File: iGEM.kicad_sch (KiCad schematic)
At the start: 57 parts, among them IC1 TMCS1107A1BQDRQ1, IC2 MCP4642-502E_UN, IC3 SN74LVC2G08IDCTRQ1, J1 COIL, J2 Conn_01x03, J3 Conn_01x02, J4 Conn_01x03, J5 Conn_01x03, J6 Conn_02x03_Odd_Even, M1 Fan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

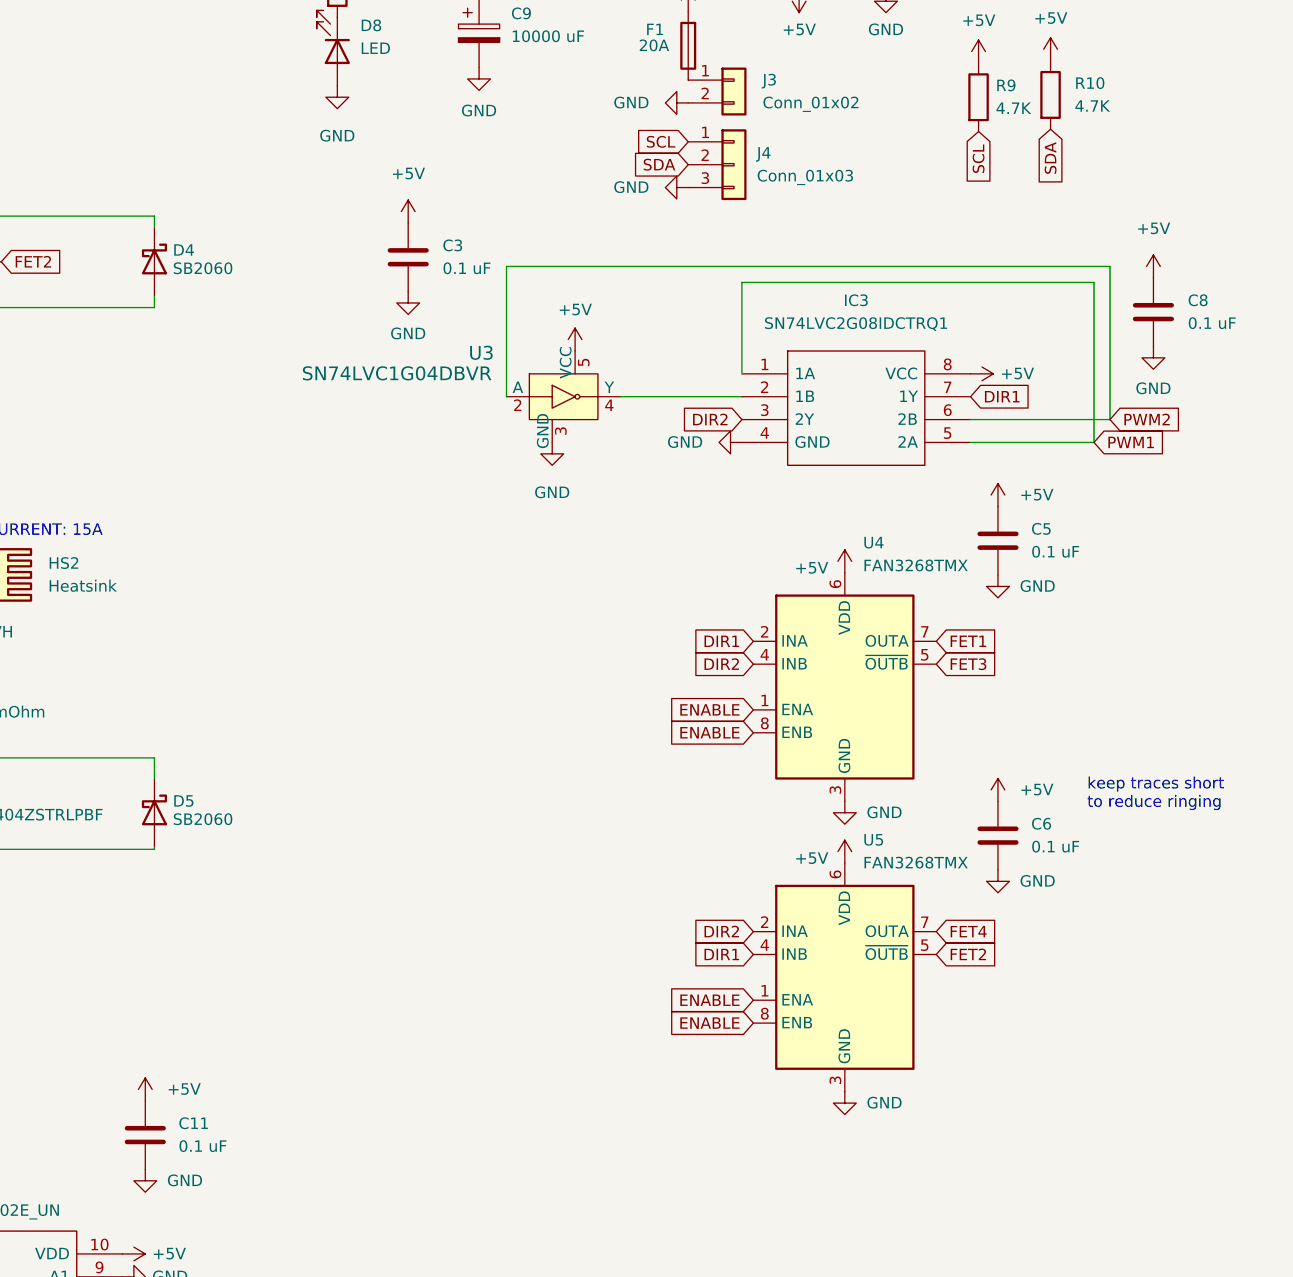
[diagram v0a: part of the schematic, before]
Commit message: MAJOR LOGIC BUG FIX. Layout also altered
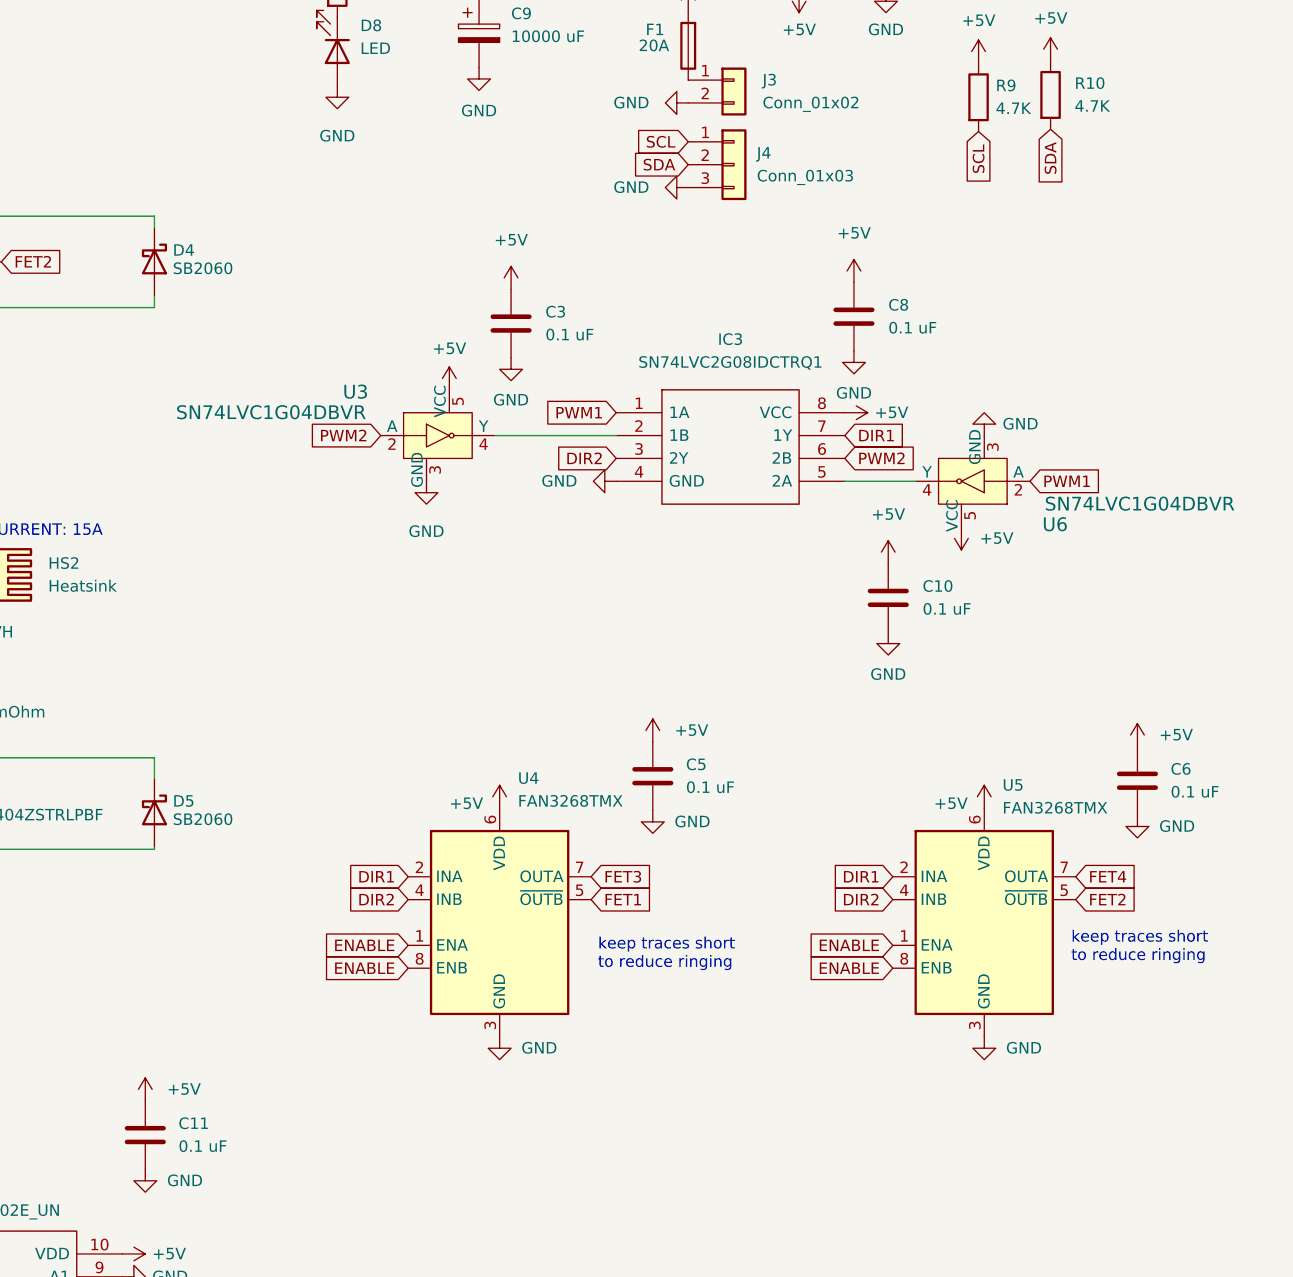
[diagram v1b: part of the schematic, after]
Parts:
- added C10: 0.1 uF, Capacitor_SMD:C_0805_2012Metric_Pad1.18x1.45mm_HandSolder, symbol Device:C
- added U6: SN74LVC1G04DBVR, digikey-footprints:SOT-753, symbol dk_Logic-Gates-and-Inverters:SN74LVC1G04DBVR
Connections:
- net +5V: now also C10.1, U6.5 (VCC)
- net DIR1: now also U5.2 (INA); no longer U5.4 (INB)
- net DIR2: now also U5.4 (INB); no longer U5.2 (INA)
- net FET1: now also U4.5 (~{OUTB}); no longer U4.7 (OUTA)
- net FET3: now also U4.7 (OUTA); no longer U4.5 (~{OUTB})
- net GND: now also C10.2, U6.3 (GND)
- net PWM1: now also U6.2 (A); no longer IC3.5 (2A)
- new net: IC3.5 (2A), U6.4 (Y)
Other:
- moved on the sheet: C3, C5, C6, C8, IC3, U3, U4, U5

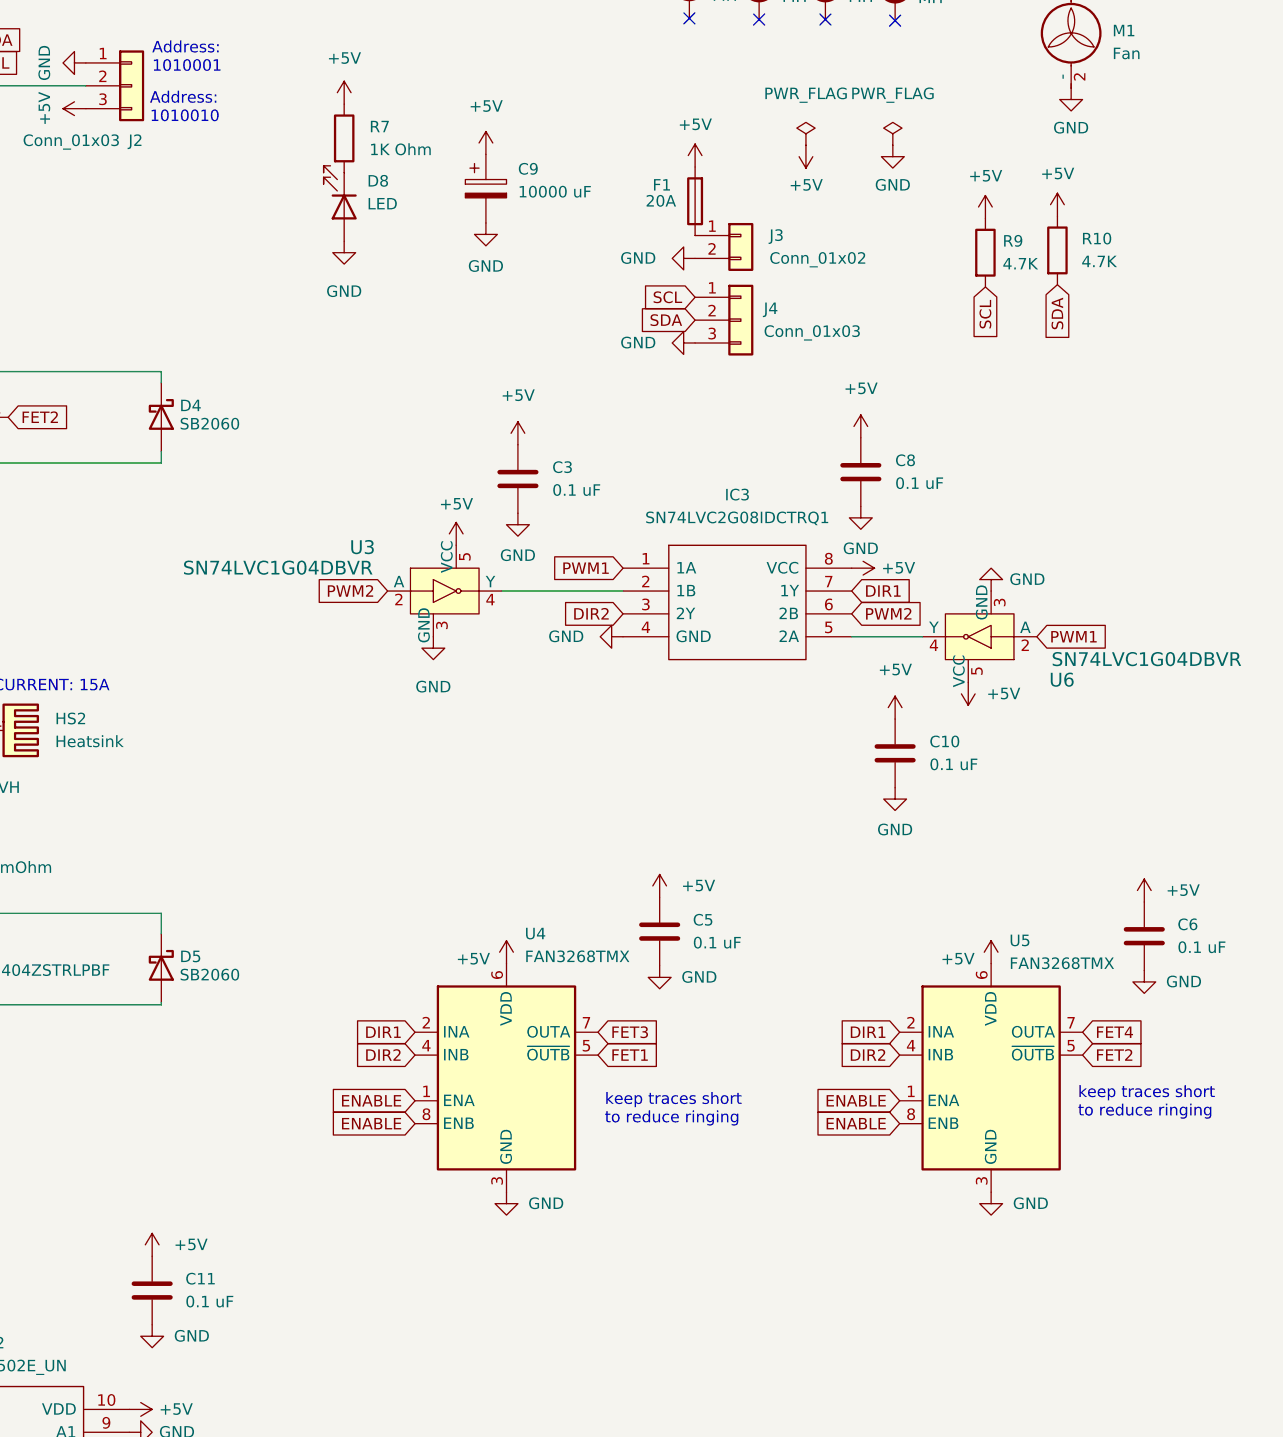
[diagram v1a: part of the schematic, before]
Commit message: Adding level shifter
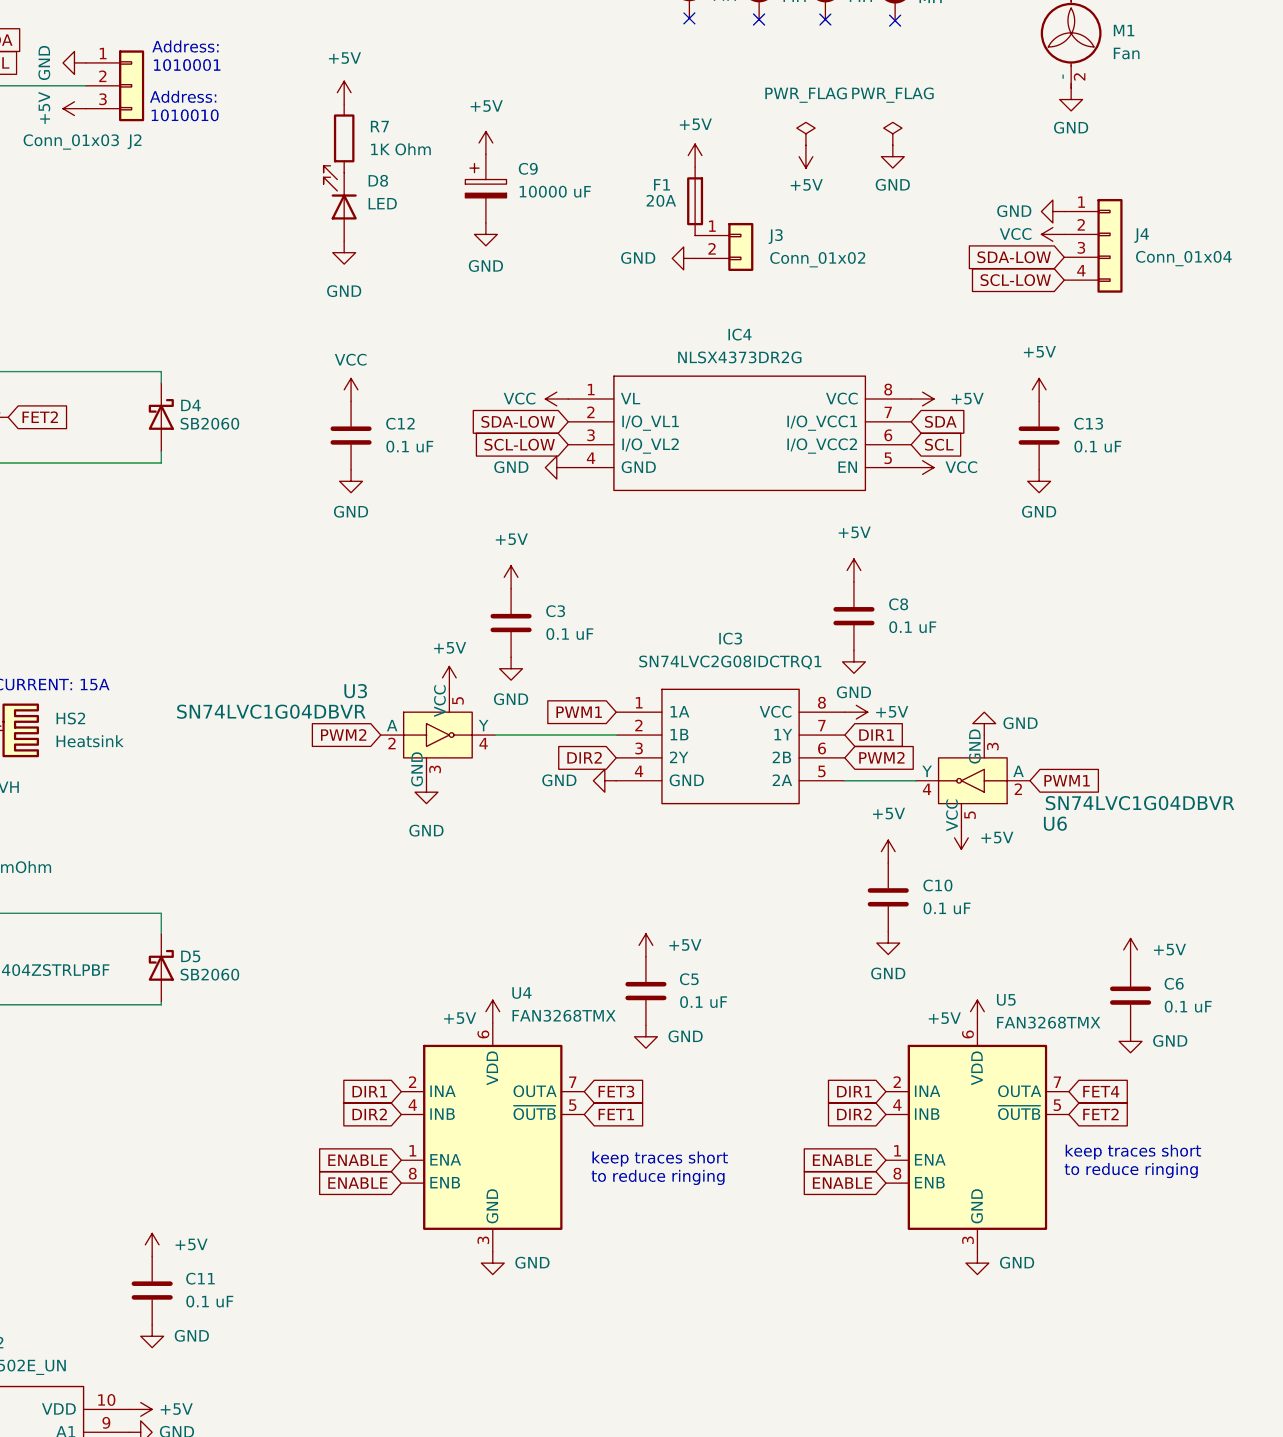
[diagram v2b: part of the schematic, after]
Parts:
- removed J4: Conn_01x03, Connector_JST:JST_XH_B3B-XH-A_1x03_P2.50mm_Vertical, symbol Connector_Generic:Conn_01x03
- removed R10, R9: 4.7K, Resistor_SMD:R_0805_2012Metric_Pad1.20x1.40mm_HandSolder, symbol Device:R
- added C12, C13: 0.1 uF, Capacitor_SMD:C_0805_2012Metric_Pad1.18x1.45mm_HandSolder, symbol Device:C
- added IC4: NLSX4373DR2G, Package_SO:SOIC-8_3.9x4.9mm_P1.27mm, symbol NLSX4373DR2G:NLSX4373DR2G
- added J4: Conn_01x04, Connector_JST:JST_SH_SM04B-SRSS-TB_1x04-1MP_P1.00mm_Horizontal, symbol Connector_Generic:Conn_01x04
- IC2: footprint SOP50P490X110-10N -> MCP4642-502E_UN:SOP50P490X110-10N
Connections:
- net +5V: now also C13.1, IC4.8 (VCC)
- net GND: now also C12.2, C13.2, IC4.4 (GND), J4.1 (Pin_1)
- net SCL: now also IC4.6 (I/O_VCC2)
- net SDA: now also IC4.7 (I/O_VCC1)
- new net SCL-LOW: IC4.3 (I/O_VL2), J4.4 (Pin_4)
- new net SDA-LOW: IC4.2 (I/O_VL1), J4.3 (Pin_3)
- new net VCC: C12.1, IC4.1 (VL), IC4.5 (EN), J4.2 (Pin_2)
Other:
- moved on the sheet: C10, C3, C5, C6, C8, IC3, U3, U4, U5, U6

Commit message: Adding inductor to prevent fan voltage spikes
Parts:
- added D9: SB2060, Diode_THT:D_DO-201AD_P12.70mm_Horizontal, symbol Device:D_Schottky
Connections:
- net +5V: now also D9.1 (K)
- net GND: now also D9.2 (A)
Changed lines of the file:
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@@
     (pin "2")
+  )
+  (symbol (lib_id "power:+5V") (at 274.066 24.638 0) (unit 1)
+    (in_bom yes) (on_board yes)
+    (property "Reference" "#PWR0132" (id 0) (at 274.066 28.448 0)
+      (effects (font (size 1.27 1.27)) hide)
+    )
+    (property "Value" "+5V" (id 1) (at 274.066 19.939 0))
+    (property "Footprint" "" (id 2) (at 274.066 24.638 0)
+      (effects (font (size 1.27 1.27)) hide)
+    )
+    (property "Datasheet" "" (id 3) (at 274.066 24.638 0)
+      (effects (font (size 1.27 1.27)) hide)
+    )
+    (pin "1")
   )
   (symbol (lib_id "Device:C") (at 201.168 91.694 0) (unit 1)
@@
     )
     (property "Datasheet" "" (id 3) (at 199.136 161.544 0)
+      (effects (font (size 1.27 1.27)) hide)
+    )
+    (pin "1")
+  )
+  (symbol (lib_id "power:GND") (at 274.066 32.258 0) (unit 1)
+    (in_bom yes) (on_board yes) (fields_autoplaced)
+    (property "Reference" "#PWR0133" (id 0) (at 274.066 38.608 0)
+      (effects (font (size 1.27 1.27)) hide)
+    )
+    (property "Value" "GND" (id 1) (at 274.066 36.703 0))
+    (property "Footprint" "" (id 2) (at 274.066 32.258 0)
+      (effects (font (size 1.27 1.27)) hide)
+    )
+    (property "Datasheet" "" (id 3) (at 274.066 32.258 0)
       (effects (font (size 1.27 1.27)) hide)
     )
@@
     (pin "9")
   )
+  (symbol (lib_id "Device:D_Schottky") (at 274.066 28.448 270) (unit 1)
+    (in_bom yes) (on_board yes)
+    (property "Reference" "D9" (id 0) (at 276.098 27.178 90)
+      (effects (font (size 1.27 1.27)) (justify left))
+    )
+    (property "Value" "SB2060" (id 1) (at 276.098 29.21 90)
+      (effects (font (size 1.27 1.27)) (justify left))
+    )
+    (property "Footprint" "Diode_THT:D_DO-201AD_P12.70mm_Horizontal" (id 2) (at 274.066 28.448 0)
+      (effects (font (size 1.27 1.27)) hide)
+    )
+    (property "Datasheet" "~" (id 3) (at 274.066 28.448 0)
+      (effects (font (size 1.27 1.27)) hide)
+    )
+    (property "DigiKey" "1655-SB2060CT-ND" (id 4) (at 274.066 28.448 90)
+      (effects (font (size 1.27 1.27)) hide)
+    )
+    (pin "1")
+    (pin "2")
+  )
   (symbol (lib_id "Device:C") (at 81.915 26.797 0) (unit 1)
     (in_bom yes) (on_board yes) (fields_autoplaced)
@@
       (reference "#PWR0131") (unit 1) (value "GND") (footprint "")
     )
+    (path "/55a24337-2e08-4fcd-be59-a76683f6410b"
+      (reference "#PWR0132") (unit 1) (value "+5V") (footprint "")
+    )
+    (path "/8c1b5342-166b-464e-9353-e3ef985f6939"
+      (reference "#PWR0133") (unit 1) (value "GND") (footprint "")
+    )
     (path "/0fbdd8b7-d3db-4cb1-9102-673f223a760c"
       (reference "C1") (unit 1) (value "0.1 uF") (footprint "Capacitor_SMD:C_0805_2012Metric_Pad1.18x1.45mm_HandSolder")
@@
       (reference "D8") (unit 1) (value "LED") (footprint "LED_SMD:LED_0805_2012Metric_Pad1.15x1.40mm_HandSolder")
     )
+    (path "/e1ac7659-7052-49b8-934f-b139f2591821"
+      (reference "D9") (unit 1) (value "SB2060") (footprint "Diode_THT:D_DO-201AD_P12.70mm_Horizontal")
+    )
     (path "/eadcb800-30ab-4a2d-bc96-28b421a136a3"

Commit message: Adding programming power protection
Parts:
- added D10: 1N5817, Diode_THT:D_DO-41_SOD81_P10.16mm_Horizontal, symbol Diode:1N5817
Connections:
- net +5V: now also D10.1 (K); no longer J6.2 (Pin_2)
- new net: D10.2 (A), J6.2 (Pin_2)
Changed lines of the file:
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@@
   )
   (symbol (lib_id "Connector_Generic:Conn_02x03_Odd_Even") (at 81.026 162.814 0) (unit 1)
-    (in_bom no) (on_board yes) (fields_autoplaced)
+    (in_bom no) (on_board yes)
     (property "Reference" "J6" (id 0) (at 82.296 153.162 0))
-    (property "Value" "Conn_02x03_Odd_Even" (id 1) (at 82.296 155.702 0))
+    (property "Value" "Conn_02x03_Odd_Even" (id 1) (at 76.708 155.956 0))
     (property "Footprint" "Connector_PinHeader_2.54mm:PinHeader_2x03_P2.54mm_Vertical" (id 2) (at 81.026 162.814 0)
       (effects (font (size 1.27 1.27)) hide)
@@
     (pin "1")
   )
-  (symbol (lib_id "power:+5V") (at 88.646 160.274 270) (unit 1)
-    (in_bom yes) (on_board yes) (fields_autoplaced)
-    (property "Reference" "#PWR047" (id 0) (at 84.836 160.274 0)
-      (effects (font (size 1.27 1.27)) hide)
-    )
-    (property "Value" "+5V" (id 1) (at 91.948 160.2739 90)
-      (effects (font (size 1.27 1.27)) (justify left))
-    )
-    (property "Footprint" "" (id 2) (at 88.646 160.274 0)
-      (effects (font (size 1.27 1.27)) hide)
-    )
-    (property "Datasheet" "" (id 3) (at 88.646 160.274 0)
+  (symbol (lib_id "power:+5V") (at 96.266 160.274 270) (unit 1)
+    (in_bom yes) (on_board yes) (fields_autoplaced)
+    (property "Reference" "#PWR047" (id 0) (at 92.456 160.274 0)
+      (effects (font (size 1.27 1.27)) hide)
+    )
+    (property "Value" "+5V" (id 1) (at 99.568 160.2739 90)
+      (effects (font (size 1.27 1.27)) (justify left))
+    )
+    (property "Footprint" "" (id 2) (at 96.266 160.274 0)
+      (effects (font (size 1.27 1.27)) hide)
+    )
+    (property "Datasheet" "" (id 3) (at 96.266 160.274 0)
       (effects (font (size 1.27 1.27)) hide)
     )
@@
     (pin "1")
   )
+  (symbol (lib_id "Diode:1N5817") (at 92.456 160.274 180) (unit 1)
+    (in_bom yes) (on_board yes) (fields_autoplaced)
+    (property "Reference" "D10" (id 0) (at 92.7735 153.67 0))
+    (property "Value" "1N5817" (id 1) (at 92.7735 156.21 0))
+    (property "Footprint" "Diode_THT:D_DO-41_SOD81_P10.16mm_Horizontal" (id 2) (at 92.456 155.829 0)
+      (effects (font (size 1.27 1.27)) hide)
+    )
+    (property "Datasheet" "http://www.vishay.com/docs/88525/1n5817.pdf" (id 3) (at 92.456 160.274 0)
+      (effects (font (size 1.27 1.27)) hide)
+    )
+    (property "DigiKey" "1N5817DICT-ND" (id 4) (at 92.456 160.274 0)
+      (effects (font (size 1.27 1.27)) hide)
+    )
+    (pin "1")
+    (pin "2")
+  )
   (symbol (lib_id "power:GND") (at 263.398 32.258 0) (unit 1)
     (in_bom yes) (on_board yes) (fields_autoplaced)
@@
       (reference "D9") (unit 1) (value "SB2060") (footprint "Diode_THT:D_DO-201AD_P12.70mm_Horizontal")
     )
+    (path "/f0c1cbd6-ee7e-45ca-9989-3cbb75ada46d"
+      (reference "D10") (unit 1) (value "1N5817") (footprint "Diode_THT:D_DO-41_SOD81_P10.16mm_Horizontal")
+    )
     (path "/eadcb800-30ab-4a2d-bc96-28b421a136a3"
